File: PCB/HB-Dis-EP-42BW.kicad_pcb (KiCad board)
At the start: 2 copper layers, 61.5 x 90 mm, 30 parts, among them J1 Reset, J2 FTDI, J4 ePaper, J6 Supply, SW0 SW_Push, SW1 SW_Push, SW10 SW_Push, SW2 SW_Push, SW3 SW_Push, SW4 SW_Push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

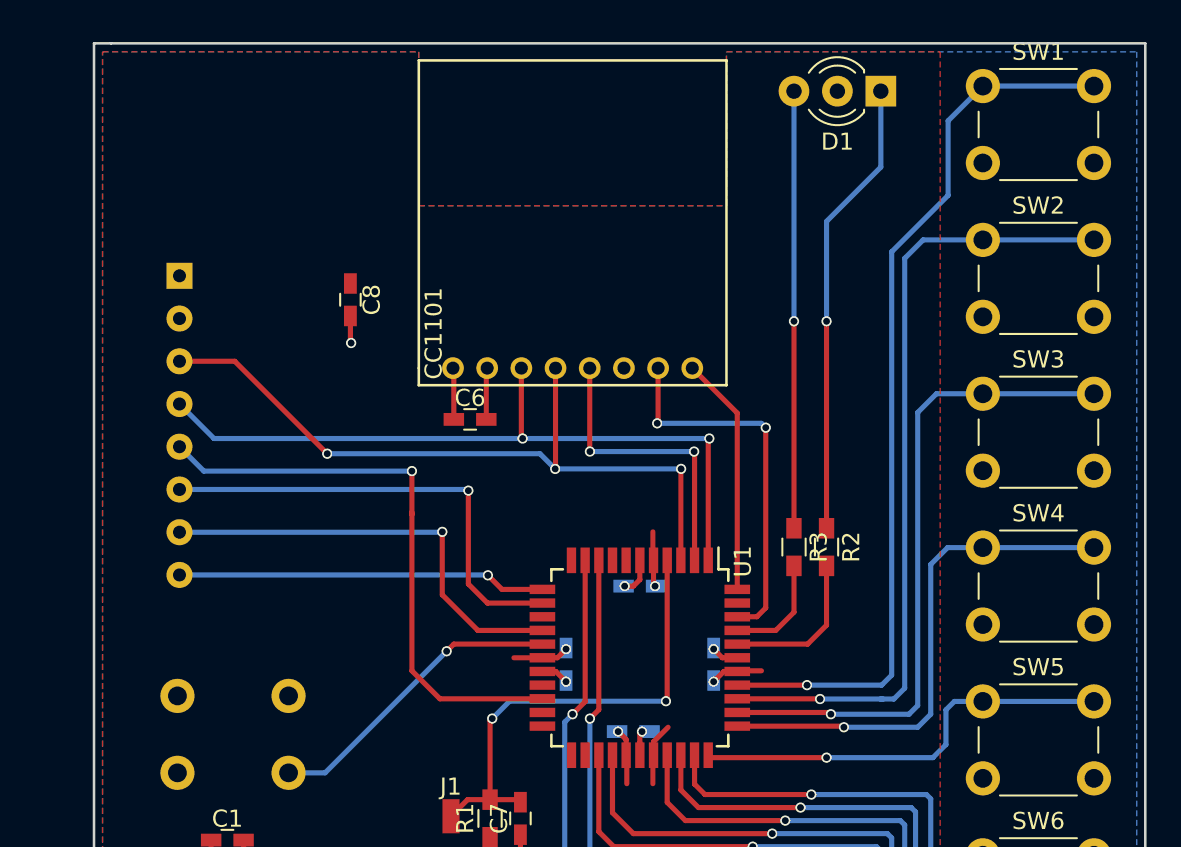
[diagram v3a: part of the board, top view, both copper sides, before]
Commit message: added opt. 8 MHz resonator
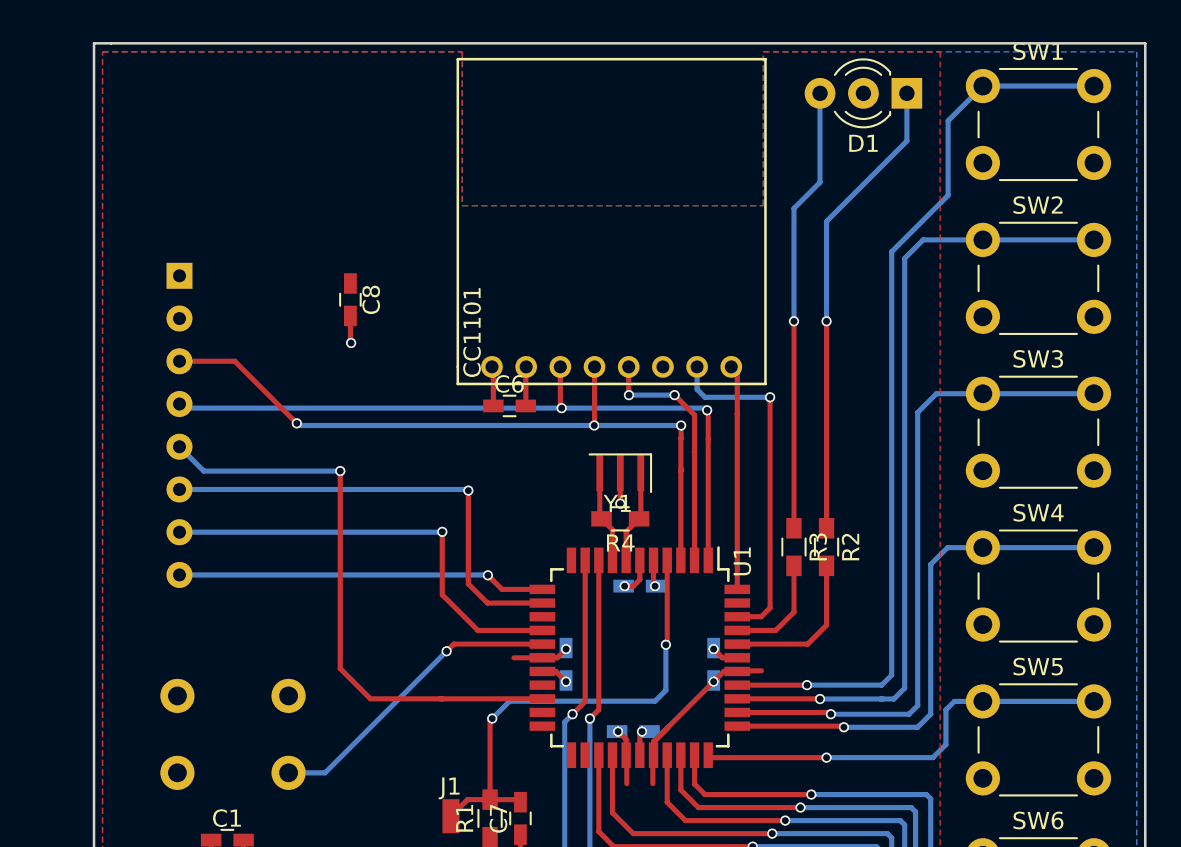
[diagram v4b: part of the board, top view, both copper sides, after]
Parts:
- added R4: 1M, Resistors_SMD:R_0603_HandSoldering, F.Cu at (89.8, 67.8)
- added Y1: Resonator, Resonators:Resonator_SMD_muRata_TPSKA-3pin_7.9x3.8mm_HandSoldering, F.Cu at (89.8, 65.2)
- moved C6 2.44 mm to (83.3, 61.2)
- moved U2 2.28 mm to (89.3, 58.9)
- moved D1 1.53 mm to (106.6, 42.9)
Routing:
- net Net-(R4-Pad2): track 0.00 -> 5.72 mm
- net Net-(R4-Pad1): track 0.00 -> 5.45 mm
- net /MISO: track 17.4 -> 14.6 mm
- net VCC: track 23.7 -> 26.4 mm
- net /GDO0: track 22.1 -> 20.2 mm, vias 2 -> 1
- net GND: track 16.8 -> 17.9 mm, vias 5 -> 6
- net /MOSI: track 43.1 -> 42.3 mm
- net /SCK: track 43.2 -> 42.4 mm
- net /CS: track 14.0 -> 13.3 mm
- net Net-(D1-Pad1): track 26.9 -> 27.4 mm
- net Net-(D1-Pad3): track 25.6 -> 26.1 mm

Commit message: replace bare ePaper by module
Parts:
- removed REF**: Waveshare_4.2inch, Waveshare_ePaper:Waveshare_4.2inch
- added R5: 10k, Resistors_SMD:R_0603_HandSoldering, F.Cu at (97.5, 63.9)
- added U3: MCP111, TO_SOT_Packages_SMD:SOT-23, F.Cu at (79.0, 85.3)
- J4: footprint CFA-10084:CFA-10084 -> Waveshare_ePaper:Waveshare_4.2inch_Module; moved to F.Cu
- moved J4 26.5 mm to (70.0, 85.3), turned to 0 degrees
- moved C8 15.5 mm to (77.4, 39.9), turned to 180 degrees
- moved D1 11.7 mm to (116.8, 37.3)
- moved J6 7.85 mm to (73.3, 89.0)
- moved C1 7.78 mm to (74.5, 85.5)
- moved J1 4.47 mm to (79.8, 80.8), turned to 270 degrees
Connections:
- J4 pad 3: /SCK -> /MOSI
- J4 pad 4: /MOSI -> /SCK
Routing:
- net /GxBSY: track 21.6 -> 52.6 mm, vias 1 -> 2
- net /GxRST: track 25.8 -> 53.1 mm
- net /GxDC: track 27.2 -> 50.8 mm, vias 1 -> 2
- net /GxCS: track 34.3 -> 54.6 mm
- net /SCK: track 42.4 -> 58.1 mm, vias 3 -> 2
- net /MOSI: track 42.3 -> 56.7 mm, vias 2 -> 3
- net Net-(D1-Pad1): track 27.4 -> 39.3 mm
- net Net-(D1-Pad3): track 26.1 -> 36.1 mm
- net GND: track 17.9 -> 22.4 mm, vias 6 -> 5
- net /RESET: track 27.8 -> 29.8 mm
- net /CS: track 13.3 -> 14.2 mm
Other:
- board size 61.5 x 90 mm -> 61.4 x 102.6 mm

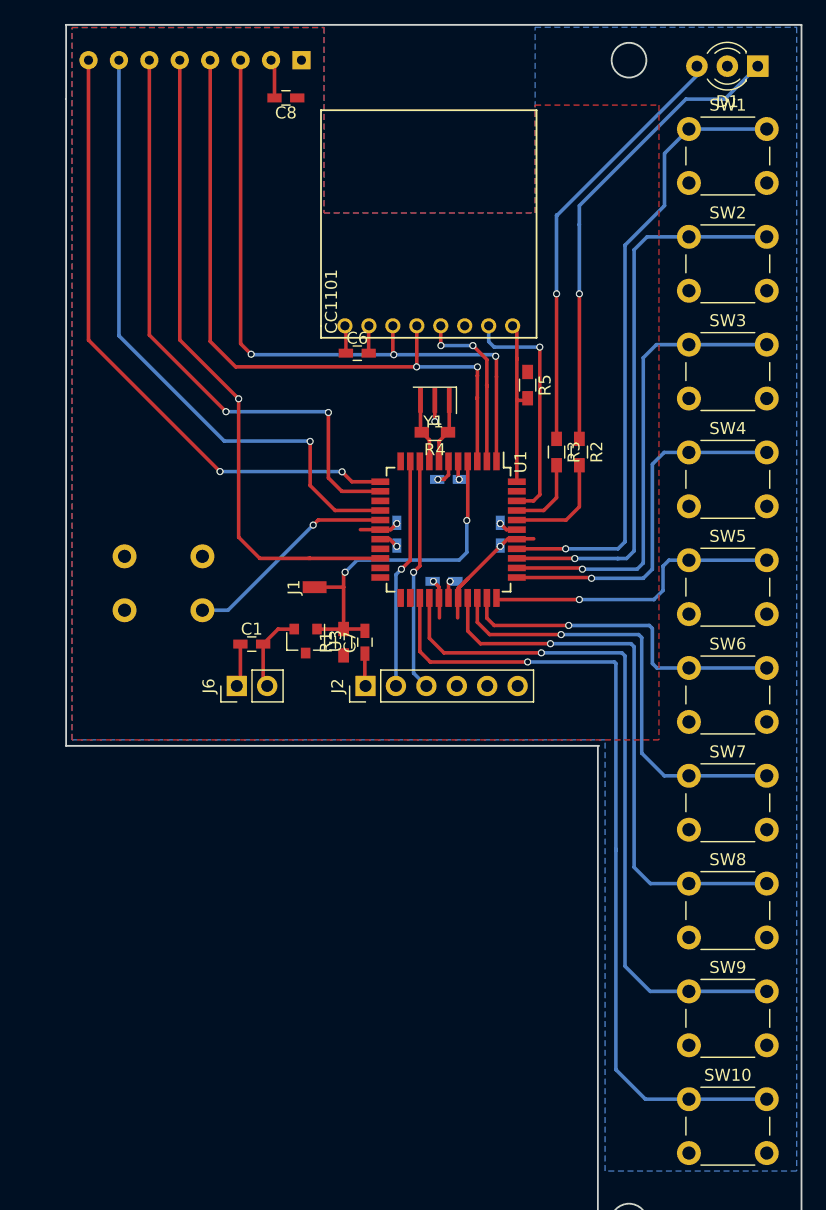
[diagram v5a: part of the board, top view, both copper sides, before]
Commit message: several improvement on PCB
- 4x GPIO for future use
- battery measurement under switchable load
- caps @ CC1101 and  @ ePaper changed to 10 uF
- extra solder points on the way to the ePaper connector
  (option to cut the upper 5 mm to fit the size of the bare ePaper)
- remove copper layers in top left, to place antenna there
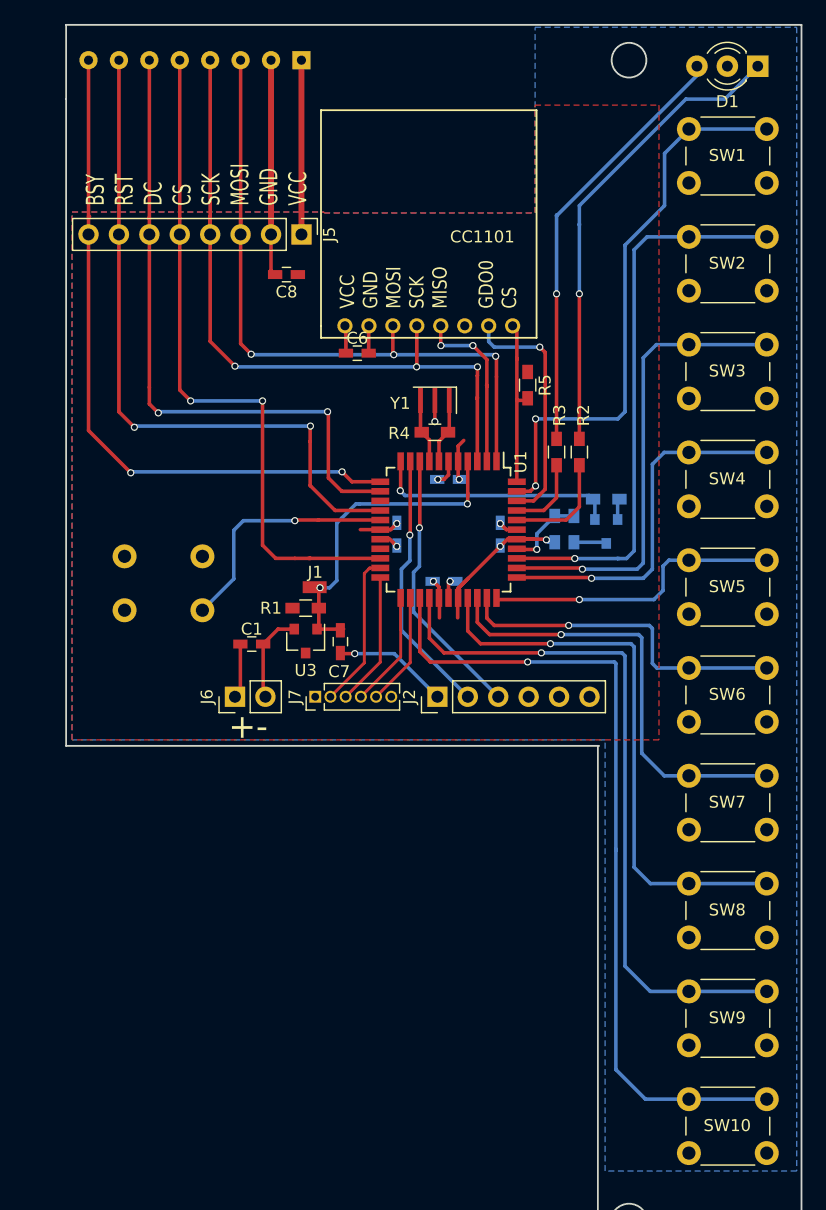
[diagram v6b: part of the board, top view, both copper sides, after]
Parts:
- added J5: ePaper_TestPoints, Pin_Headers:Pin_Header_Straight_1x08_Pitch2.54mm, F.Cu at (78.7, 51.3)
- added J7: GeneralPurpose, Pin_Headers:Pin_Header_Straight_1x06_Pitch1.27mm, F.Cu at (79.8, 89.9)
- added Q1: IRLML6344, TO_SOT_Packages_SMD:SOT-23, B.Cu at (104.1, 76.1)
- added R6: 4k7, Resistors_SMD:R_0603_HandSoldering, B.Cu at (104.1, 73.4)
- added R7: 8.2, Resistors_SMD:R_0603_HandSoldering, B.Cu at (99.8, 75.9)
- added R8: 8.2, Resistors_SMD:R_0603_HandSoldering, B.Cu at (101.4, 75.9)
- C6, C8: value 100n -> 10u
- moved C8 14.8 mm to (77.4, 54.7)
- moved J2 6.07 mm to (90.0, 89.9)
- moved R1 4.26 mm to (79.0, 82.5), turned to 0 degrees
- moved C7 2.05 mm to (81.9, 85.3)
- moved J6 0.91 mm to (73.1, 89.9)
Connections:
- U1 pad 11: Net-(U1-Pad11) -> /BI_EN
- U1 pad 21: Net-(U1-Pad21) -> /GPIO0
- U1 pad 22: Net-(U1-Pad22) -> /GPIO1
- U1 pad 23: Net-(U1-Pad23) -> /GPIO2
- U1 pad 24: Net-(U1-Pad24) -> /GPIO3
- U1 pad 37: /BTN1 -> /BI_MEAS
- U1 pad 43: Net-(U1-Pad43) -> /BTN1
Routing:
- net VCC: track 26.1 -> 46.8 mm, vias 4 -> 5
- net /BI_EN: track 0.00 -> 20.6 mm, vias 0 -> 1
- net GND: track 22.4 -> 40.2 mm
- net /GPIO0: track 0.00 -> 13.0 mm
- net /GPIO1: track 0.00 -> 11.2 mm
- net /GPIO2: track 0.00 -> 9.63 mm
- net /GPIO3: track 0.00 -> 9.44 mm
- net /DTR: track 2.73 -> 9.61 mm, vias 0 -> 1
- net /BI_MEAS: track 0.00 -> 6.71 mm, vias 0 -> 1
- net /BTN1: track 52.5 -> 47.4 mm, vias 1 -> 2
- net /GxBSY: track 52.6 -> 57.3 mm
- net /GxRST: track 53.1 -> 57.6 mm, vias 1 -> 2
- net /GxDC: track 50.8 -> 54.5 mm
- net /RX: track 19.4 -> 22.9 mm
- net /TX: track 19.2 -> 22.3 mm
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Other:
- board text added: "+-"
- board text added: "BSY RST DC CS SCK MOSI GND VCC"
- board text added: "ToDo: - move config button / optionally place below SW10?"
- board text added: "VCC GND MOSI SCK MISO GDO0 CS"

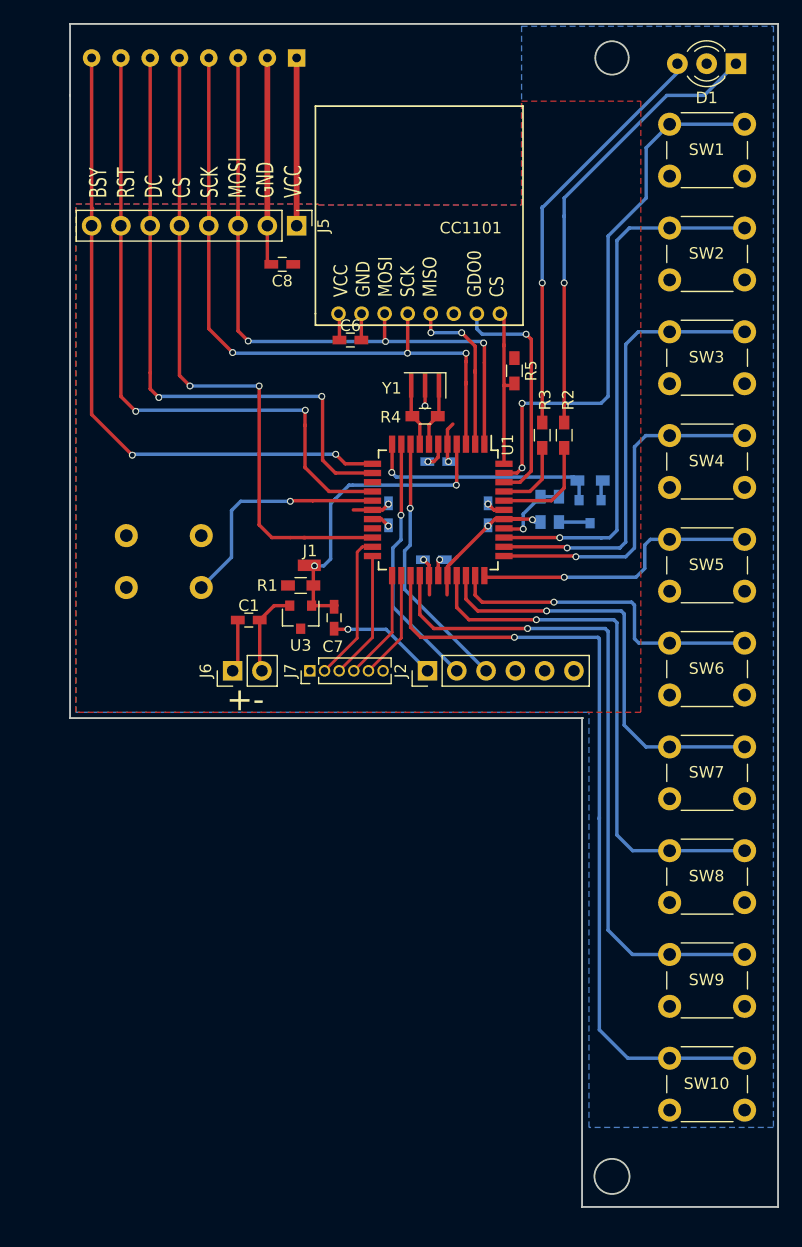
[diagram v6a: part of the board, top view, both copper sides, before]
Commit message: further improvements to PCB
- change caps @ CC1101 and @ ePaper to 1 uF
- shrink GPIOs to 3
- add I²C connecter for future use
- move config button to desired place and add hole for optional head-over-heels mounting
- add 6-pin JTAG header on backside
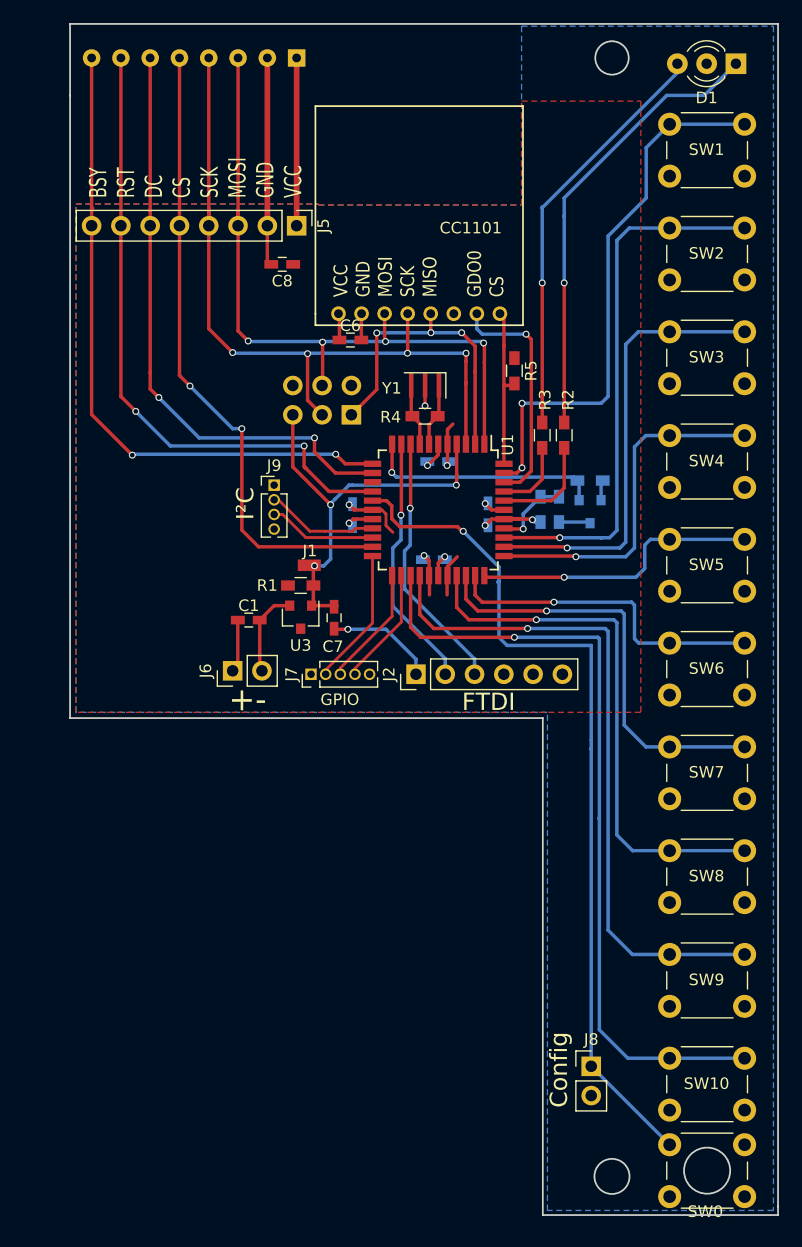
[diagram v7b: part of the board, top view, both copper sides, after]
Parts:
- added J3: ISP, Pin_Headers:Pin_Header_Straight_2x03_Pitch2.54mm, B.Cu at (83.4, 67.7)
- added J8: Config, Pin_Headers:Pin_Header_Straight_1x02_Pitch2.54mm, F.Cu at (104.2, 124.2)
- added J9: Conn_I2C, Pin_Headers:Pin_Header_Straight_1x04_Pitch1.27mm, F.Cu at (76.7, 73.8)
- C6, C8: value 10u -> 1u
- J7: value GeneralPurpose -> Conn_GPIO; footprint Pin_Headers:Pin_Header_Straight_1x06_Pitch1.27mm -> Pin_Headers:Pin_Header_Straight_1x05_Pitch1.27mm
- SW0: moved to F.Cu
- moved SW0 67.5 mm to (111.0, 131.0)
- moved C3 3.11 mm to (83.5, 76.4)
- moved J2 1.04 mm to (89.0, 90.2)
- moved J7 0.32 mm to (79.9, 90.2)
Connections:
- J7 pad 2: /GPIO0 -> /GPIO1
- J7 pad 3: /GPIO1 -> /GPIO2
- J7 pad 4: /GPIO2 -> /GPIO3
- J7 pad 5: /GPIO3 -> GND
- U1 pad 19: Net-(U1-Pad19) -> /SCL
- U1 pad 20: /GxCS -> /SDA
- U1 pad 21: /GPIO0 -> /GxCS
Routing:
- net /CONFIG: track 20.3 -> 74.7 mm
- net /GPIO0: track 13.0 -> 0.00 mm
- net /MISO: track 14.6 -> 27.3 mm, vias 2 -> 3
- net /SCL: track 0.00 -> 9.77 mm
- net /SDA: track 0.00 -> 9.36 mm
- net /RESET: track 27.8 -> 37.0 mm, vias 2 -> 3
- net /SCK: track 59.7 -> 65.6 mm, vias 3 -> 4
- net /MOSI: track 58.0 -> 61.9 mm, vias 3 -> 4
- net /GxDC: track 54.5 -> 51.9 mm
- net /GxRST: track 57.6 -> 55.9 mm
- net /GxCS: track 57.4 -> 55.7 mm
- net GND: track 40.2 -> 41.4 mm
- net /GPIO3: track 9.44 -> 10.2 mm
- net /GPIO2: track 9.63 -> 10.4 mm
- net /GPIO1: track 11.2 -> 11.9 mm
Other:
- board size 61.4 x 102.6 mm -> 61.4 x 103.3 mm
- board text added: "Config"
- board text added: "FTDI"
- board text added: "GPIO"
- board text added: "I²C"
- board text added: "JTAG"
- board text added: "config button can be mounted from the front or head-over-heels on the back through the hole then drill a small hole in the back of the case"
- board text removed: "ToDo: - move config button / optionally place below SW10?"
- board text removed: "config button on backside drill small hole in the back of the case"
